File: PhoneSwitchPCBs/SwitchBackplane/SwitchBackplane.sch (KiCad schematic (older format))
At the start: 155 parts

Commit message: Fix library table entries
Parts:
- removed Q?: XP231N02013R-G, Package_TO_SOT_SMD:SOT-323_SC-70_Handsoldering, symbol PhoneInterfaceParts:XP231N02013R-G
- added Q?: XP231N02013R-G, Package_TO_SOT_SMD:SOT-323_SC-70_Handsoldering, symbol PhoneInterfaceParts:XP231N02013R-G
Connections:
- net GND: now also Q?.2 (S)
- net at IC?.1 (~SD), IC?.2 (~FAULT), R?.2: now also Q?.3 (D)
- net at R?.1, R?.2: now also Q?.1 (G)
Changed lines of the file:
@@
-	1    0    0    -1
-$EndComp
-$Comp
-L PhoneInterfaceParts:XP231N02013R-G Q?
-U 1 1 69235CAD
-P 2800 6775
-F 0 "Q?" H 3005 6821 50  0000 L CNN
-F 1 "XP231N02013R-G" H 3005 6730 50  0000 L CNN
-F 2 "Package_TO_SOT_SMD:SOT-323_SC-70_Handsoldering" H 3000 6700 50  0001 L CIN
-F 3 "https://www.torexsemi.com/file/XP231N02013R/XP231N02013R.pdf" H 2800 6775 50  0001 L CNN
-	1    2800 6775
 	1    0    0    -1
 $EndComp
@@
 Wire Wire Line
 	2975 6975 2900 6975
-Connection ~ 2900 6975
 Wire Wire Line
 	3225 6975 3225 7075
@@
 Text Label 2200 6575 2    50   ~ 0
 RGE
+$Comp
+L PhoneInterfaceParts:XP231N02013R-G Q?
+U 1 1 613E0C8E
+P 2800 6775
+F 0 "Q?" H 3005 6821 50  0000 L CNN
+F 1 "XP231N02013R-G" H 3005 6730 50  0000 L CNN
+F 2 "Package_TO_SOT_SMD:SOT-323_SC-70_Handsoldering" H 3000 6700 50  0001 L CIN
+F 3 "" H 2800 6775 50  0001 L CNN
+	1    2800 6775
+	1    0    0    -1
+$EndComp
+Connection ~ 2900 6975
 $EndSCHEMATC

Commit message: Update notes and progress more on schematic
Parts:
- added C? (x3): .1u, symbol Device:C_Small
- added C?: 30p, symbol Device:C_Small
- added IC?: MT8870DS1, Package_SO:SOIC-18W_7.5x11.6mm_P1.27mm, symbol Imported_Parts:MT8870DS1
- added Q?: PMV65XP, Package_TO_SOT_SMD:SOT-23, symbol SwitchBackplaneParts:PMV65XP
- added R? (x3): 10, symbol Device:R_Small
- added SW?: System Reset, symbol Switch:SW_Push
- added U1: Pi Pico, RPi_Pico:RPi_Pico_SMD_TH, symbol MCU_RaspberryPi_and_Boards:Pico
- added Y?: 3.579545 MHz, symbol Device:Crystal_Small
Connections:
- wire segments 772 -> 832
- no-connect marks 0 -> 3

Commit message: Continue work on schematic
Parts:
- removed C? (x2): .1u, symbol Device:C_Small
- removed R?: 10, symbol Device:R_Small
- added C? (x6): .1u, symbol Device:C_Small
- added C? (x4): 2.2u, symbol Device:C_Small
- added D? (x2): PMBD7000, Package_TO_SOT_SMD:SOT-23, symbol SwitchBackplaneParts:PMBD7000
- added IC?: MT8870DS1, Package_SO:SOIC-18W_7.5x11.6mm_P1.27mm, symbol Imported_Parts:MT8870DS1
- added IC? (x3): XRA1403IG24TR-F, Package_SO:TSSOP-24_4.4x7.8mm_P0.65mm, symbol Imported_Parts:XRA1403IG24TR-F
- added Q? (x10): XP231N02013R-G, Package_TO_SOT_SMD:SOT-323_SC-70_Handsoldering, symbol PhoneInterfaceParts:XP231N02013R-G
- added R? (x2): 100k, symbol Device:R_Small
- added R? (x2): 300k, symbol Device:R_Small
- added R? (x20): 10k, symbol Device:R_Small
- added R? (x2): 600, symbol Device:R_Small
- R? (x2): value 10 -> 100k
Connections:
- net labels added: 350A, 350B, 440A, 440B, 480A, 480B, 620A, 620B, AE8, DA1, DA2, DA3, DA4, DB1, DB2, DB3, DB4, DH1, DH2, DL1, DL2, MISO, MOSI, SCK, T1, T2
- wire segments 832 -> 1062
- no-connect marks 3 -> 10
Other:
- note added: "Tone Gen / Decoders"
- note removed: "Call-Progress Tone Generators"
- moved on the sheet: C?, D?, F?, FB?, IC?, J?, PS?, Q?, R?, RV?, T?, U?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

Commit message: Clarify pin counts and fix notes error, continue work on schematic
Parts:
- removed SW?: System Reset, symbol Switch:SW_Push
- added C?: .1u, symbol Device:C_Small
- added IC?: XRA1403IG24TR-F, Package_SO:TSSOP-24_4.4x7.8mm_P0.65mm, symbol Imported_Parts:XRA1403IG24TR-F
- added J? (x2): Trunk 1, symbol Connector_Generic:Conn_02x11_Odd_Even
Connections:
- net labels added: CSMC, CSR1, CSR2, CST, TA1, TA2, TCI1, TCI2, THS1, THS2, TLG1, TLG2, TLS1, TLS2, TRT1, TRT2
- wire segments 1062 -> 1180
- no-connect marks 10 -> 15
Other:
- moved on the sheet: C?, D?, F?, IC?, J?, PS?, Q?, R?, U1, U?

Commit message: More work on schematics
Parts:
- removed C? (x3): 4.7u, symbol Device:CP_Small
- added C? (x5): 4.7u, symbol Device:C_Small
- added D?: PWR, symbol Device:LED_Small
- added D? (x10): RE1, symbol Device:LED_Small
- added D? (x11): RT1, symbol Device:LED_Small
- added R?: 1.5k, symbol Device:R_Small
- added R? (x21): 180, symbol Device:R_Small
- C? (x2): value 1u -> 4.7u
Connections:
- net +12V: now also C?.1, C?.1, R?.1
- net +3V3: now also R?.1
- net +5VA: now also C?.1
- net +5VD: now also C?.1
- net -5VA: now also C?.2
- net GND: now also C?.1, C?.2, C?.2, C?.2, C?.2, D?.1 (K), D?.1 (K), D?.1 (K), D?.1 (K), D?.1 (K), D?.1 (K), D?.1 (K), D?.1 (K), D?.1 (K), D?.1 (K), D?.1 (K), D?.1 (K), D?.1 (K), D?.1 (K), D?.1 (K), D?.1 (K), D?.1 (K), D?.1 (K), D?.1 (K), D?.1 (K), D?.1 (K)
- net RE1: now also R?.1
- net RE2: now also R?.1
- net RE3: now also R?.1
- net RE4: now also R?.1
- net RE5: now also R?.1
- net RE6: now also R?.1
- net RE7: now also R?.1
- net RE8: now also R?.1
- net RGE: now also D?.1 (K)
- net RT1: now also R?.1
- net RT2: now also R?.1
- net RT3: now also R?.1
- net RT4: now also R?.1
- net RT5: now also R?.1
- net RT6: now also R?.1
- net RT7: now also R?.1
- net RT8: now also R?.1
- net TA1: now also R?.1
- net TA2: now also R?.1
- net TRT1: now also R?.1
- net TRT2: now also R?.1
- new net: D?.2 (A), R?.2 (x22)
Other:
- note added: "Indicator LEDs"
- moved on the sheet: C?, D?, F?, J?, PS?, Q?, R?, U1, U?

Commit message: Further work on schematic, rearranged some things on IO expander ICs
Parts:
- removed R? (x2): 600, symbol Device:R_Small
- added J?: SWD, symbol Connector_Generic:Conn_01x03
- added J?: UART, symbol Connector_Generic:Conn_01x03
- J?: value Trunk 1 -> Trunk 2
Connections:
- net +12V: no longer J?.19 (Pin_19), J?.19 (Pin_19)
- net AE1: now also IC?.13 (P8); no longer IC?.5 (P1)
- net AE2: now also IC?.14 (P9); no longer IC?.9 (P5)
- net AE3: now also IC?.15 (P10); no longer IC?.14 (P9)
- net AE4: now also IC?.16 (P11); no longer IC?.18 (P13)
- net AE5: now also IC?.17 (P12); no longer IC?.5 (P1)
- net AE6: now also IC?.18 (P13); no longer IC?.9 (P5)
- net AE7: now also IC?.19 (P14); no longer IC?.14 (P9)
- net AE8: now also IC?.20 (P15); no longer IC?.18 (P13)
- net GND: now also J?.19 (Pin_19), J?.19 (Pin_19), J?.1 (Pin_1), J?.1 (Pin_1)
- net LG1: now also IC?.4 (P0); no longer IC?.6 (P2)
- net LG2: now also IC?.5 (P1); no longer IC?.10 (P6)
- net LG3: now also IC?.6 (P2); no longer IC?.15 (P10)
- net LG4: now also IC?.7 (P3); no longer IC?.19 (P14)
- net LG5: now also IC?.8 (P4); no longer IC?.6 (P2)
- net LG6: now also IC?.9 (P5); no longer IC?.10 (P6)
- net LG7: now also IC?.10 (P6); no longer IC?.15 (P10)
- net LG8: now also IC?.11 (P7); no longer IC?.19 (P14)
- net PC1: now also IC?.13 (P8); no longer IC?.7 (P3)
- net PC2: now also IC?.14 (P9); no longer IC?.11 (P7)
- net PC3: now also IC?.15 (P10); no longer IC?.16 (P11)
- net PC4: now also IC?.16 (P11); no longer IC?.20 (P15)
- net PC5: now also IC?.17 (P12); no longer IC?.7 (P3)
- net PC6: now also IC?.18 (P13); no longer IC?.11 (P7)
- net PC7: now also IC?.19 (P14); no longer IC?.16 (P11)
- net RE2: now also IC?.5 (P1); no longer IC?.8 (P4)
- net RE3: now also IC?.6 (P2); no longer IC?.13 (P8)
- net RE4: now also IC?.7 (P3); no longer IC?.17 (P12)
- net RE5: now also IC?.8 (P4); no longer IC?.4 (P0)
- net RE6: now also IC?.9 (P5); no longer IC?.8 (P4)
- net RE7: now also IC?.10 (P6); no longer IC?.13 (P8)
- net RE8: now also IC?.11 (P7); no longer IC?.17 (P12)
- net TA1: now also IC?.15 (P10); no longer IC?.14 (P9)
- net TA2: now also IC?.16 (P11); no longer IC?.18 (P13)
- net TCI2: now also IC?.14 (P9); no longer IC?.17 (P12)
- net TLG1: now also IC?.17 (P12); no longer IC?.15 (P10)
- net TLG2: now also IC?.18 (P13); no longer IC?.19 (P14)
- net TLS1: now also IC?.19 (P14); no longer IC?.16 (P11)
- net at U1.1 (GPIO0): now also J?.2 (Pin_2)
- net at U1.2 (GPIO1): now also J?.3 (Pin_3)
- net at U1.41 (SWCLK): now also J?.3 (Pin_3)
- net at U1.43 (SWDIO): now also J?.2 (Pin_2)
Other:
- note added: "Trunks + Module Presence Detect"
- moved on the sheet: C?, IC?, Q?, U1

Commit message: Start to finish up schematic, add PDF of current schematic revision
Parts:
- added C? (x2): 100u, symbol Device:CP_Small
- added C? (x2): .001u, symbol Device:C_Small
- added C? (x2): .1u, symbol Device:C_Small
- F?: value 150mA -> 100mA
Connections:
- net +12V: now also C?.1, C?.1, C?.2, C?.2, C?.2, C?.2
- net GND: now also C?.1, C?.1, C?.1, C?.1, C?.2, C?.2
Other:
- note added: "MCU"
- moved on the sheet: C?, D?, F?, IC?, J?, PS?, Q?, R?, U1, U?

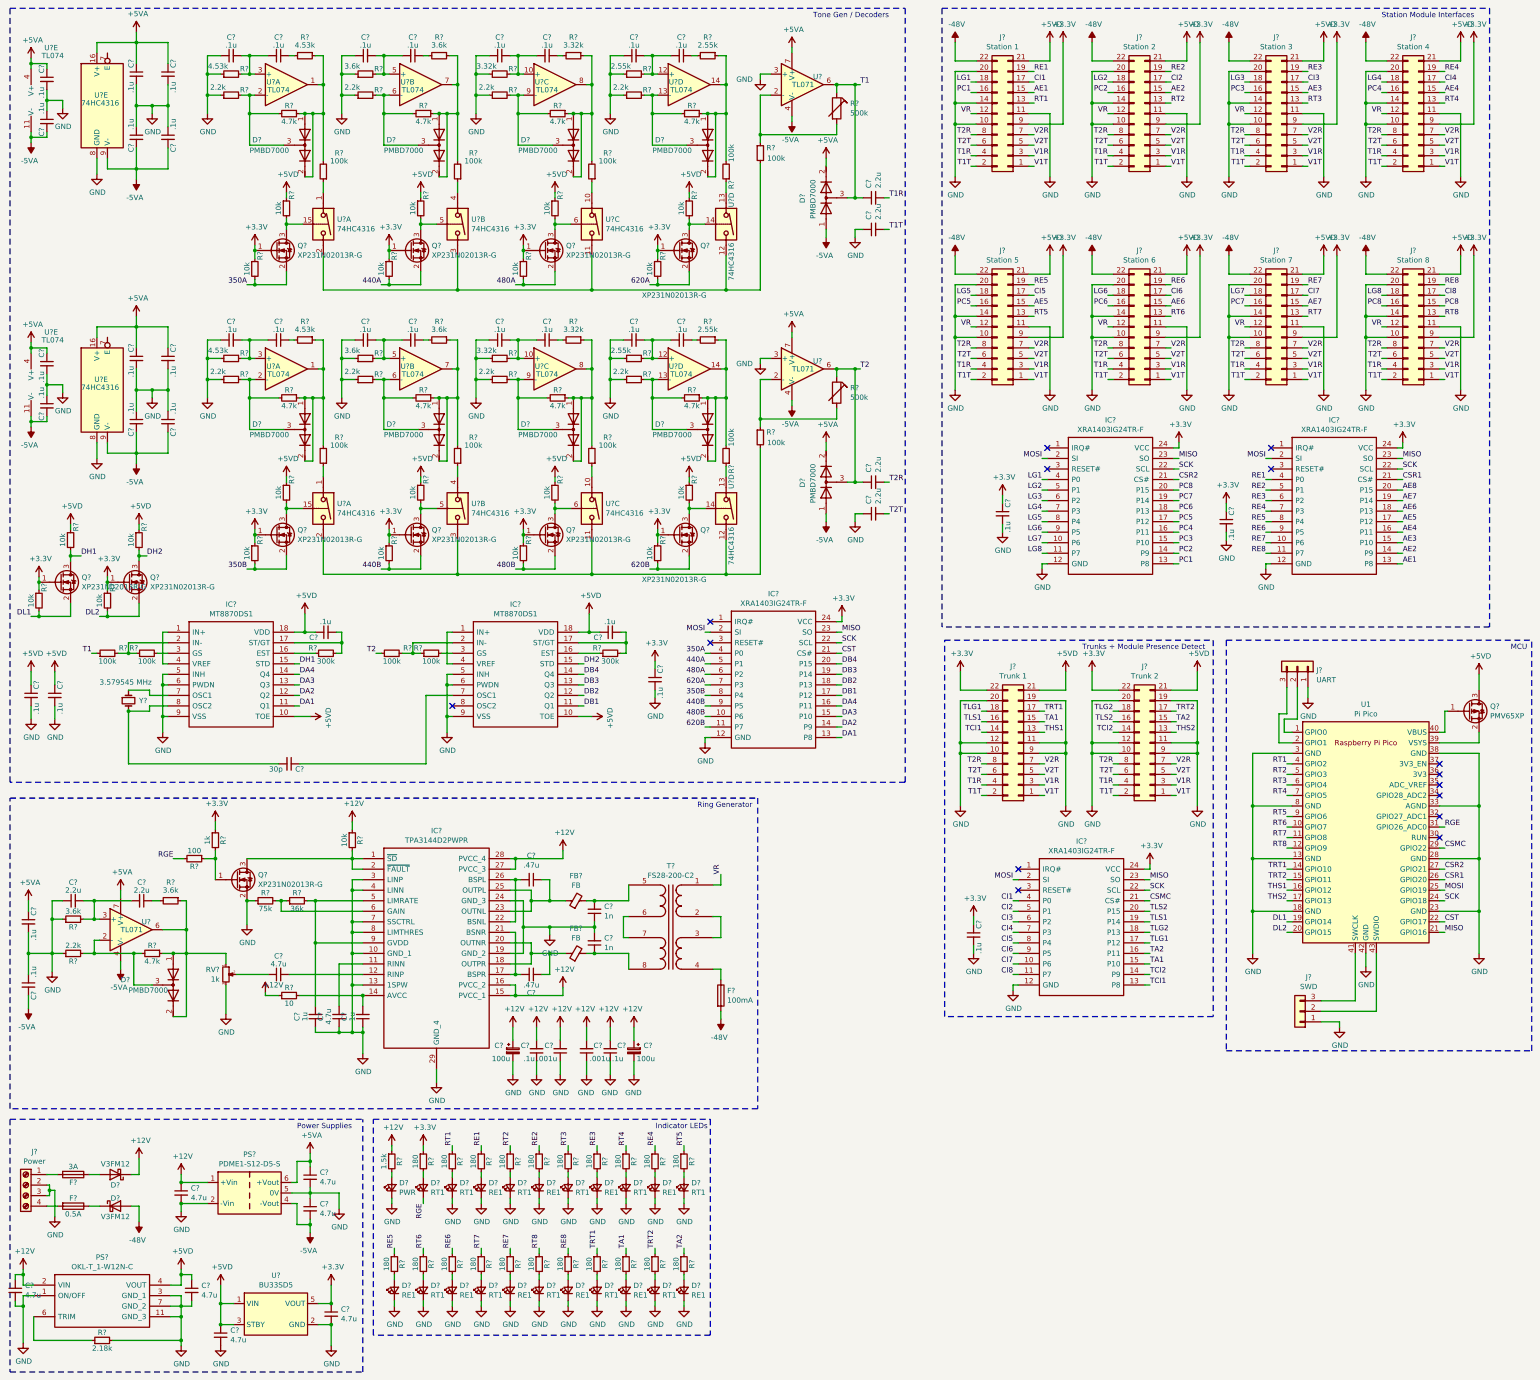
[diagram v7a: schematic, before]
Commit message: Fixed a few small issues, annotated schematic, cleaned up annotations, fixed issue with switch ICs
The annotations were a mess, cleaned them all up. Also modified some components so the ERC would stop complaining.  Fixed the issue with forgetting to connect switch IC enable, and finally made all the ICs Ux.
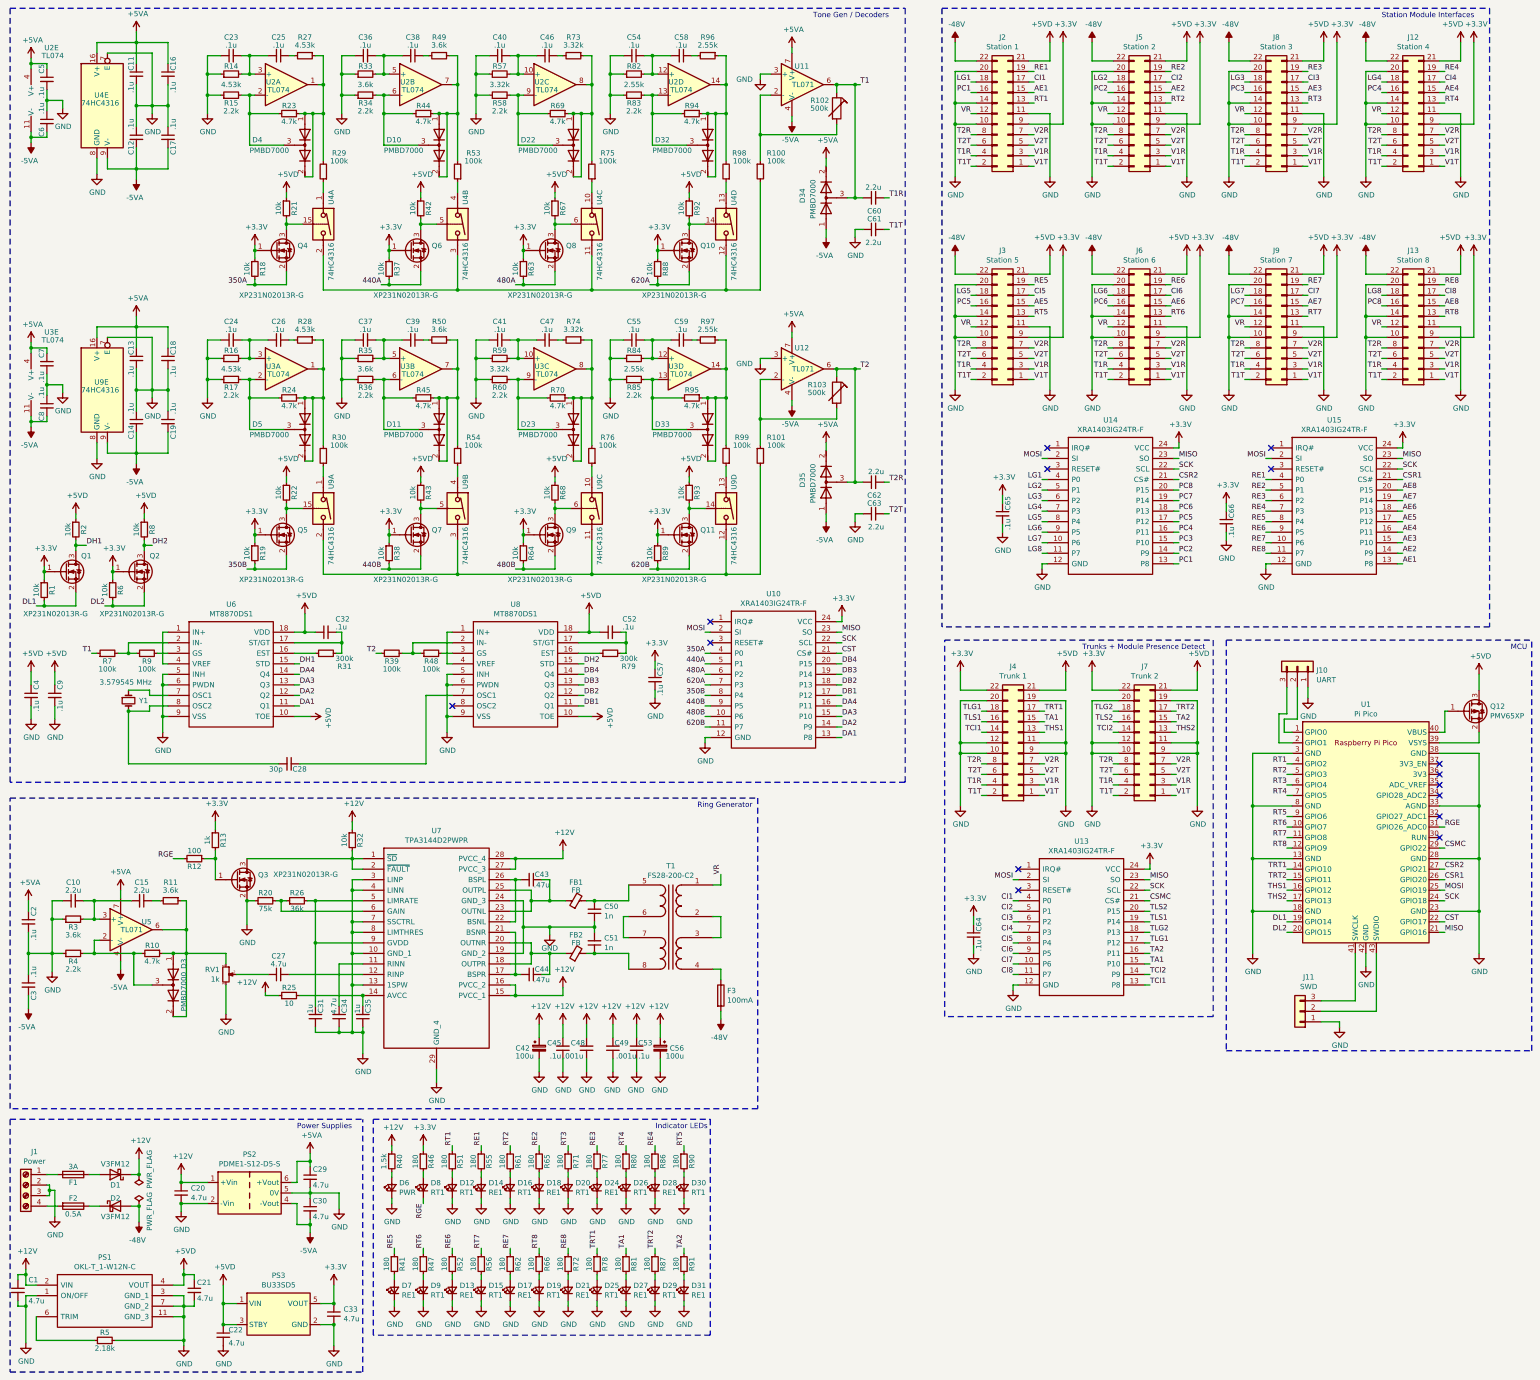
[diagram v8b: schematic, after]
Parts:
- gave numbers to parts that had none: 254
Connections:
- net +5VA: now also U9.16 (V+); no longer U4.16 (V+)
- net -5VA: now also U9.9 (V-); no longer U4.9 (V-)
- net AE8: now also J13.15 (Pin_15)
- net GND: now also U4.7 (E), U9.7 (E), U9.8 (GND); no longer U4.8 (GND)
- net PC8: no longer J13.15 (Pin_15)
- net at R29.1: now also U4.1; no longer U9.1
- net at Q4.3 (D), R21.2: now also U4.15; no longer U9.15
- net at R53.1: now also U4.4; no longer U4.4
- net at Q6.3 (D), R42.2: now also U4.5; no longer U4.5
- net at R75.1: now also U4.10; no longer U9.10
- net at Q8.3 (D), R67.2: now also U4.6; no longer U9.6
- net at R98.1: now also U4.13; no longer U9.13
- net at Q10.3 (D), R92.2: now also U4.14; no longer U9.14
- net at R99.1: now also U9.13; no longer U4.13
- net at Q11.3 (D), R93.2: now also U9.14; no longer U4.14
- net at R54.1: now also U9.4; no longer U4.4
- net at Q7.3 (D), R43.2: now also U9.5; no longer U4.5
- net at R30.1: now also U9.1; no longer U9.1
- net at Q5.3 (D), R22.2: now also U9.15; no longer U9.15
- new net: R101.2, U9.11, U9.12, U9.2, U9.3
- new net: R100.2, U4.11, U4.12, U4.2, U4.3
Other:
- moved on the sheet: C1, C21, C22, C33, C42, C45, C48, C49, C53, C56, PS1, PS3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
